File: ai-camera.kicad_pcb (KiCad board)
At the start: 4 copper layers, 70 x 70 mm, 166 parts, among them J1 Conn-01x02_P2mm_S2B-PH-K-S_Ho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, J2 USB_B_Micro_10118194-0001LF, J3 DBG, J4 Conn-02x10_P2.54mm_B-2100S20P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, J5 Conn-01x02_P1.25mm_10114829-1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, J6 Conn_01x24_FFC_0.5mm_hirose_F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, J7 Conn_01x24_FFC_0.5mm_hirose_F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, Q1 AO3401A, Q2 AO3400A, Q3 AO3400A, Q4 AO3401A, Q5 AO3400A, Q6 AO3401A, Q7 AO3400A, Q8 AO3400A, SW1 SW_PB_TS-1187A-B-A-B, SW2 SW_PB_TS-1187A-B-A-B, SW3 SW_PB_TS-1187A-B-A-B, SW4 SW_PB_TS-1187A-B-A-B, U1 SRV05-4, U10 AP1511B, U11 ESP32-S3-WROOM-1-N16R8, U12 MT9284-28J, U2 TP4057-42-SOT26-R, U3 PCF8563T/5,518, U4 XC6206-2.8V, U5 PIR_BS612, U6 SY8089AAAC, U7 SOT-23-6_SN74LVC1G373DBVR_TI, U8 XC6206-2.8V, U9 RT9166-12GVL, Y1 32.768kHz_Q13FC1350000400

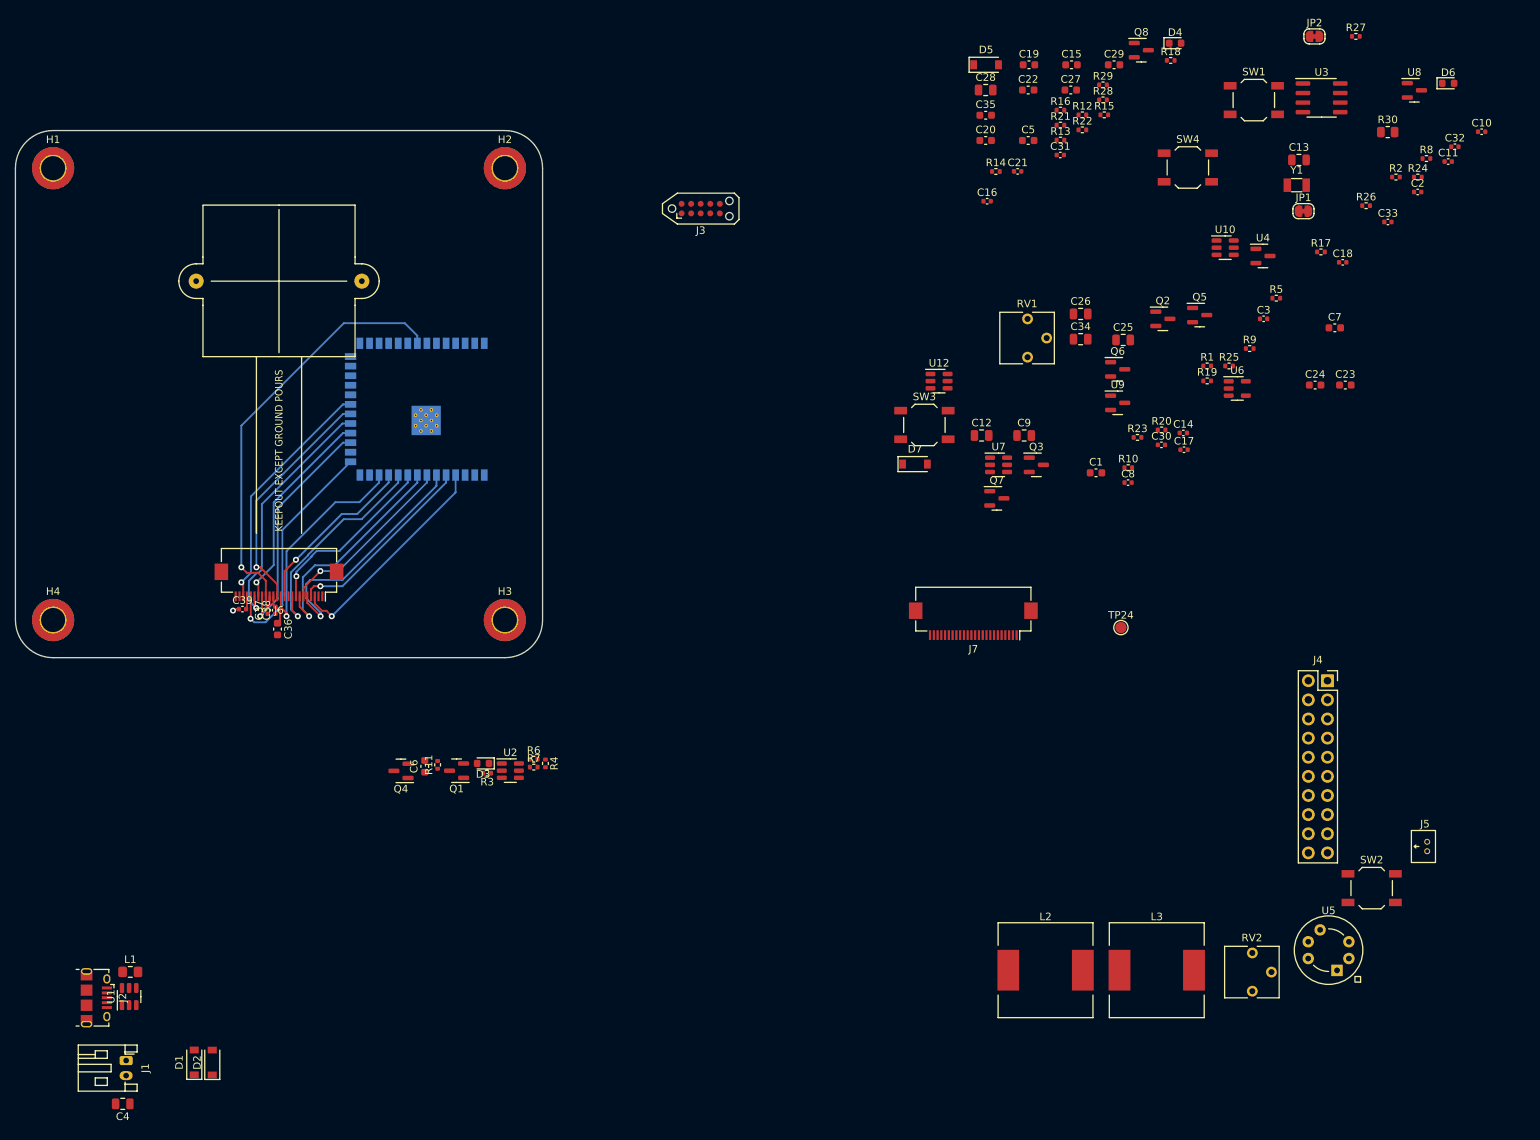
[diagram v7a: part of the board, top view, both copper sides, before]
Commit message: ai camera layout: prelim USB, PIR, PIR cfg, battery, ML connector
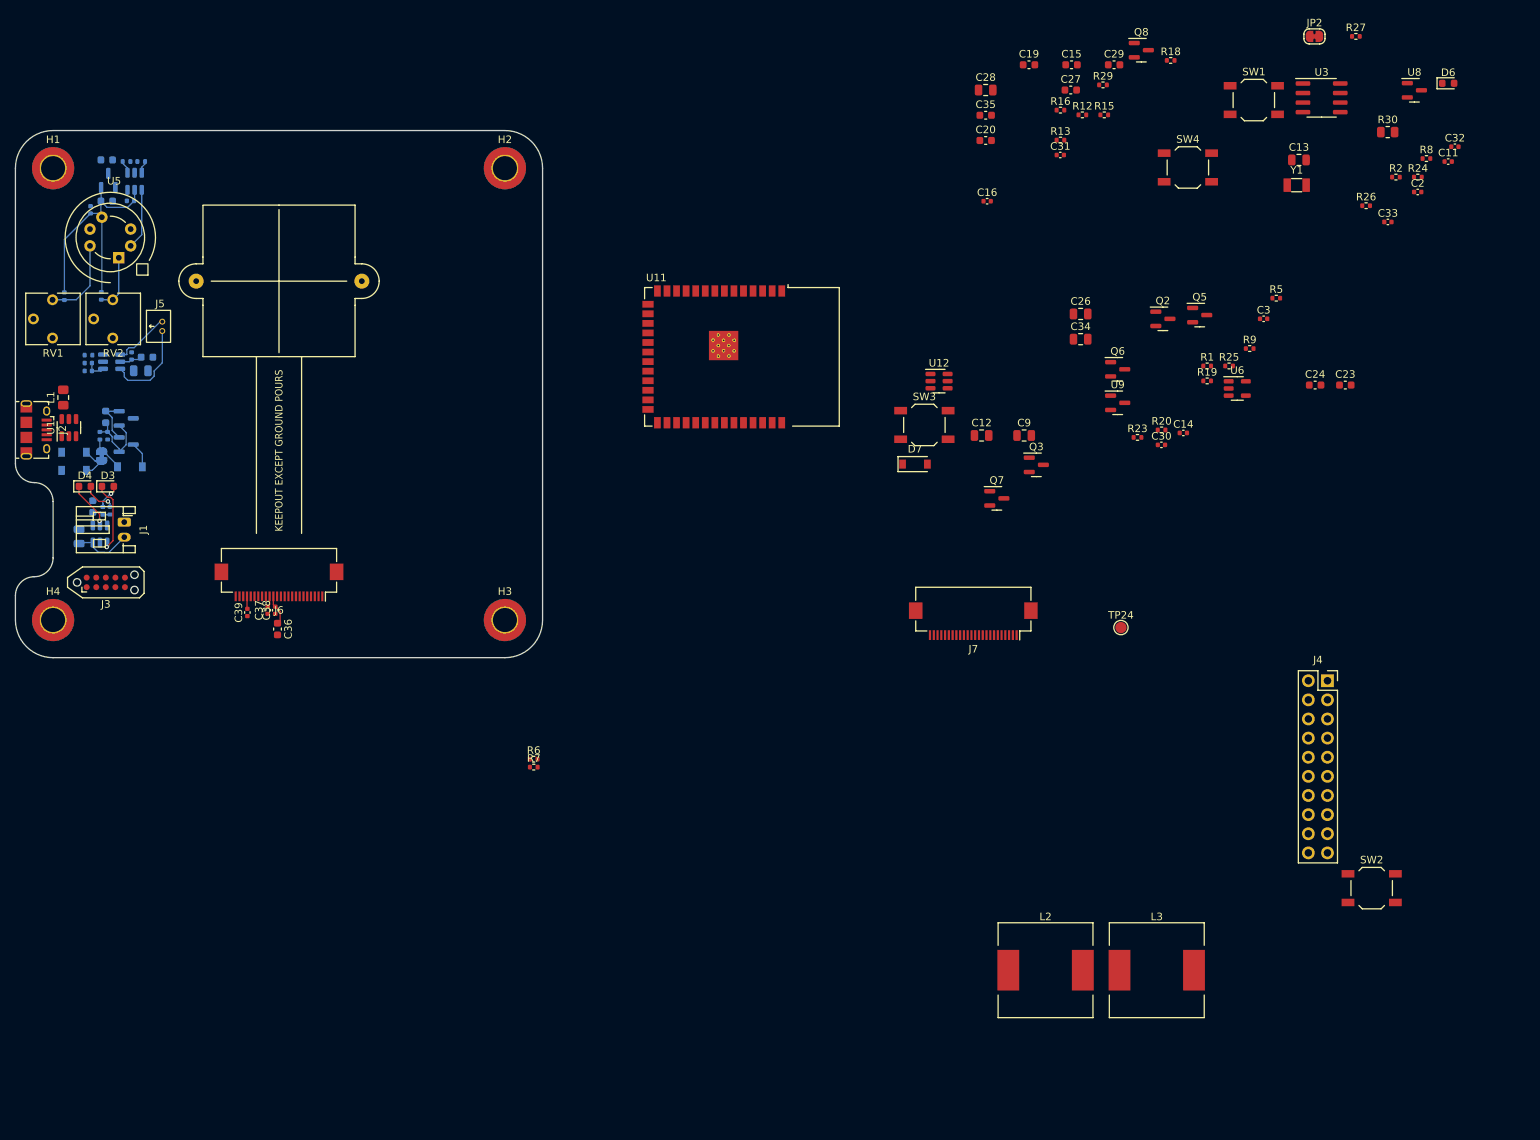
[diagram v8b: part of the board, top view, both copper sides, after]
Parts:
- C1, C10, C17, C18, C21, C22, C25, C4, C5, C6, C7, C8, D1, D2, D5, JP1, Q1, Q4, R10, R11, R14, R17, R21, R22, R28, R3, R4, U10, U2, U4, U7: moved to B.Cu
- U11: moved to F.Cu
- moved U5 187.4 mm to (107.6, 59.2)
- moved J5 181.6 mm to (114.0, 71.0)
- moved C10 179.7 mm to (110.3, 54.3), turned to 180 degrees
- moved RV2 177.0 mm to (107.9, 67.5), turned to 180 degrees
- moved C18 167.1 mm to (104.7, 75.9), turned to 180 degrees
- moved C7 163.9 mm to (107.1, 54.4)
- moved JP1 162.9 mm to (106.5, 88.2), turned to -90 degrees
- moved R17 162.1 mm to (106.4, 67.0), turned to -90 degrees
- moved D4 156.3 mm to (104.2, 92.2)
- moved U4 153.7 mm to (107.3, 51.6), turned to 90 degrees
- moved U10 148.6 mm to (107.8, 75.7)
- moved C17 145.9 mm to (104.7, 76.9), turned to 180 degrees
- moved C8 142.5 mm to (105.0, 55.5), turned to 90 degrees
- moved R28 138.9 mm to (104.7, 74.8)
- moved R10 135.6 mm to (107.2, 85.5), turned to -90 degrees
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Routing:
- net /CAM.HREF: track 55.6 -> 0.00 mm, vias 1 -> 0
- net /PWR_PIR: track 0.00 -> 34.2 mm
- net /CAM.RST: track 32.9 -> 0.00 mm, vias 1 -> 0
- net /CAM.D5: track 32.6 -> 0.00 mm, vias 1 -> 0
- net /CAM.SDA: track 32.2 -> 0.00 mm, vias 1 -> 0
- net /CAM.D9: track 31.4 -> 0.00 mm, vias 1 -> 0
- net /CAM.PWDN: track 31.4 -> 0.00 mm, vias 1 -> 0
- net /CAM.SCL: track 31.2 -> 0.00 mm, vias 1 -> 0
- net /CAM.D6: track 30.1 -> 0.00 mm, vias 1 -> 0
- net /CAM.D4: track 29.5 -> 0.00 mm, vias 1 -> 0
- net /CAM.D7: track 29.4 -> 0.00 mm, vias 1 -> 0
- net /CAM.MCLK: track 28.7 -> 0.00 mm, vias 1 -> 0
- net /CAM.VSYNC: track 27.5 -> 0.00 mm, vias 1 -> 0
- net /CAM.D3: track 25.7 -> 0.00 mm, vias 1 -> 0
- net /CAM.D2: track 24.3 -> 0.00 mm, vias 1 -> 0
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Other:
- outline, holes or cut-outs redrawn
